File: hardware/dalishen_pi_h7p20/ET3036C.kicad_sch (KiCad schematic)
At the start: 29 parts, among them U6 EA3036C

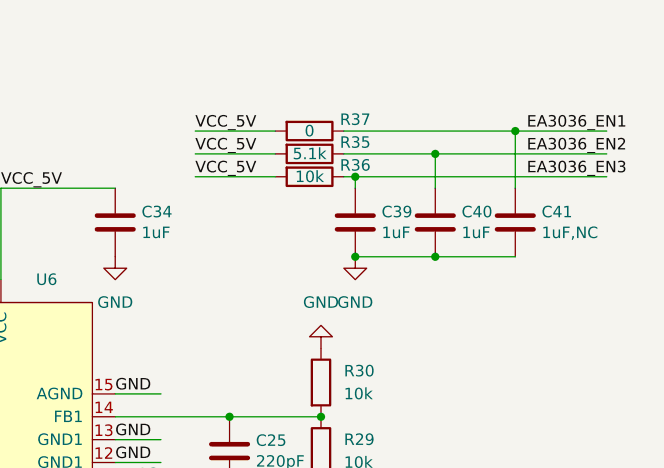
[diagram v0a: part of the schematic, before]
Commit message: [usb_sniffer_h7p20] 结构优化与验证
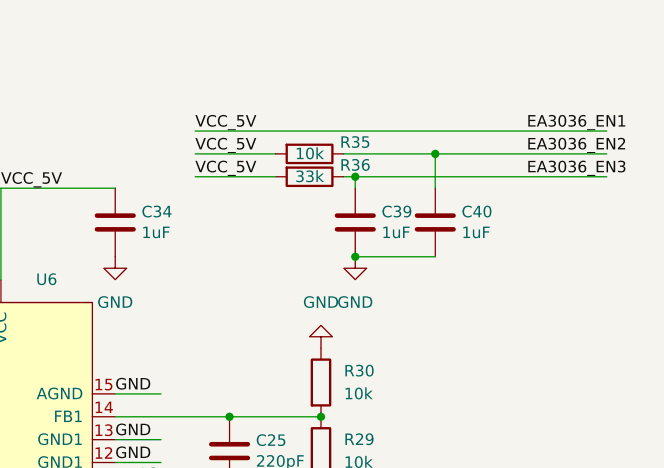
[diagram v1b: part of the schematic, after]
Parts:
- removed C41: 1uF,NC, Capacitor_SMD:C_0402_1005Metric, symbol Device:C
- removed R37: 0, Resistor_SMD:R_0402_1005Metric, symbol Device:R
- R35: value 5.1k -> 10k
- R36: value 10k -> 33k
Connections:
- net EA3036_EN1 is gone; now on net VCC_5V: U6.9 (EN1)
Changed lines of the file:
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@@
   (junction (at 182.88 93.98) (diameter 0) (color 0 0 0 0)
   )
-  (junction (at 204.47 62.23) (diameter 0) (color 0 0 0 0)
-  )
   (junction (at 172.72 93.98) (diameter 0) (color 0 0 0 0)
   )
@@
   (junction (at 111.76 88.9) (diameter 0) (color 0 0 0 0)
   )
-  (junction (at 195.58 76.2) (diameter 0) (color 0 0 0 0)
-  )
   (junction (at 114.3 118.11) (diameter 0) (color 0 0 0 0)
   )
@@
     (stroke (width 0) (type default))
   )
-  (wire (pts (xy 168.91 62.23) (xy 177.8 62.23))
-    (stroke (width 0) (type default))
-  )
   (wire (pts (xy 114.3 118.11) (xy 123.19 118.11))
     (stroke (width 0) (type default))
@@
     (stroke (width 0) (type default))
   )
-  (wire (pts (xy 204.47 68.58) (xy 204.47 62.23))
-    (stroke (width 0) (type default))
-  )
   (wire (pts (xy 182.88 101.6) (xy 191.77 101.6))
     (stroke (width 0) (type default))
@@
     (stroke (width 0) (type default))
   )
-  (wire (pts (xy 195.58 76.2) (xy 204.47 76.2))
-    (stroke (width 0) (type default))
-  )
   (wire (pts (xy 168.91 67.31) (xy 177.8 67.31))
     (stroke (width 0) (type default))
@@
     (stroke (width 0) (type default))
   )
-  (wire (pts (xy 204.47 62.23) (xy 214.63 62.23))
-    (stroke (width 0) (type default))
-  )
   (wire (pts (xy 160.02 96.52) (xy 165.1 96.52))
     (stroke (width 0) (type default))
   )
-  (wire (pts (xy 185.42 62.23) (xy 204.47 62.23))
+  (wire (pts (xy 168.91 62.23) (xy 214.63 62.23))
     (stroke (width 0) (type default))
   )
@@
       (effects (font (size 1.27 1.27)))
     )
-    (property "Value" "10k" (at 181.61 67.31 90)
+    (property "Value" "33k" (at 181.61 67.31 90)
       (effects (font (size 1.27 1.27)))
     )
@@
         (path "/221176f3-b6da-4f04-afa6-f8c6dd49907a/bd4c9780-8757-4d43-90d3-516996f3c3ef"
           (reference "C39") (unit 1)
-        )
-      )
-    )
-  )
-  (symbol (lib_id "Device:C") (at 204.47 72.39 180) (unit 1)
-    (in_bom yes) (on_board yes) (dnp no)
-    (property "Reference" "C41" (at 207.391 71.2216 0)
-      (effects (font (size 1.27 1.27)) (justify right))
-    )
-    (property "Value" "1uF,NC" (at 207.391 73.533 0)
-      (effects (font (size 1.27 1.27)) (justify right))
-    )
-    (property "Footprint" "Capacitor_SMD:C_0402_1005Metric" (at 203.5048 68.58 0)
-      (effects (font (size 1.27 1.27)) hide)
-    )
-    (property "Datasheet" "~" (at 204.47 72.39 0)
-      (effects (font (size 1.27 1.27)) hide)
-    )
-    (pin "1")
-    (pin "2")
-    (instances
-      (project "dalishen_pi_h7p20"
-        (path "/221176f3-b6da-4f04-afa6-f8c6dd49907a/bd4c9780-8757-4d43-90d3-516996f3c3ef"
-          (reference "C41") (unit 1)
-        )
-      )
-    )
-  )
-  (symbol (lib_id "Device:R") (at 181.61 62.23 270) (unit 1)
-    (in_bom yes) (on_board yes) (dnp no)
-    (property "Reference" "R37" (at 186.69 60.96 90)
-      (effects (font (size 1.27 1.27)))
-    )
-    (property "Value" "0" (at 181.61 62.23 90)
-      (effects (font (size 1.27 1.27)))
-    )
-    (property "Footprint" "Resistor_SMD:R_0402_1005Metric" (at 181.61 60.452 90)
-      (effects (font (size 1.27 1.27)) hide)
-    )
-    (property "Datasheet" "~" (at 181.61 62.23 0)
-      (effects (font (size 1.27 1.27)) hide)
-    )
-    (pin "1")
-    (pin "2")
-    (instances
-      (project "dalishen_pi_h7p20"
-        (path "/221176f3-b6da-4f04-afa6-f8c6dd49907a/bd4c9780-8757-4d43-90d3-516996f3c3ef"
-          (reference "R37") (unit 1)
         )
       )
@@
       (effects (font (size 1.27 1.27)))
     )
-    (property "Value" "5.1k" (at 181.61 64.77 90)
-      (effects (font (size 1.27 1.27)))
-    )
+    (property "Value" "10k" (at 181.61 64.77 90)
+      (effects (font (size 1.27 1.27)))
+    )

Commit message: [dalishen_pi_h7p20] backup
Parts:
- R29, R30, R31, R32, R33, R34, R35: value 10k -> 10k,1%
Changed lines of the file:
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@@
       (effects (font (size 1.27 1.27)) (justify left))
     )
-    (property "Value" "10k" (at 105.41 93.98 0)
+    (property "Value" "10k,1%" (at 105.41 93.98 0)
       (effects (font (size 1.27 1.27)) (justify left))
     )
@@
       (effects (font (size 1.27 1.27)) (justify left))
     )
-    (property "Value" "10k" (at 116.84 115.57 0)
+    (property "Value" "10k,1%" (at 116.84 115.57 0)
       (effects (font (size 1.27 1.27)) (justify left))
     )
@@
       (effects (font (size 1.27 1.27)) (justify left))
     )
-    (property "Value" "10k" (at 185.42 91.44 0)
+    (property "Value" "10k,1%" (at 185.42 91.44 0)
       (effects (font (size 1.27 1.27)) (justify left))
     )
@@
       (effects (font (size 1.27 1.27)) (justify left))
     )
-    (property "Value" "10k" (at 116.84 123.19 0)
+    (property "Value" "10k,1%" (at 116.84 123.19 0)
       (effects (font (size 1.27 1.27)) (justify left))
     )
@@
       (effects (font (size 1.27 1.27)) (justify left))
     )
-    (property "Value" "10k" (at 185.42 99.06 0)
+    (property "Value" "10k,1%" (at 185.42 99.06 0)
       (effects (font (size 1.27 1.27)) (justify left))
     )
@@
       (effects (font (size 1.27 1.27)) (justify left))
     )
-    (property "Value" "10k" (at 105.41 86.36 0)
+    (property "Value" "10k,1%" (at 105.41 86.36 0)
       (effects (font (size 1.27 1.27)) (justify left))
     )
@@
       (effects (font (size 1.27 1.27)))
     )
-    (property "Value" "10k" (at 181.61 64.77 90)
-      (effects (font (size 1.27 1.27)))
-    )
+    (property "Value" "10k,1%" (at 181.61 64.77 90)
+      (effects (font (size 1.27 1.27)))
+    )

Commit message: [dalishen_pi_h7p20] 原理图初稿
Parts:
- removed C25, C28, C35: 220pF, Capacitor_SMD:C_0402_1005Metric, symbol Device:C
- removed C26, C27, C29, C30, C31, C32, C33, C36, C37: 10uF, Capacitor_SMD:C_0402_1005Metric, symbol Device:C
- removed C34, C39, C40: 1uF, Capacitor_SMD:C_0402_1005Metric, symbol Device:C
- removed L3, L4, L5: 1.5uH, vllogic:L_NR3015, symbol Device:L
- removed R29, R30, R31, R32, R33, R34, R35: 10k,1%, Resistor_SMD:R_0402_1005Metric, symbol Device:R
- removed R36: 33k, Resistor_SMD:R_0402_1005Metric, symbol Device:R
- removed U6: EA3036C, Package_DFN_QFN:QFN-20-1EP_3x3mm_P0.4mm_EP1.65x1.65mm, symbol vllogic_chip:EA3036C
